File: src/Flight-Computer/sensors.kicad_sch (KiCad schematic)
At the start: 37 parts, among them P4 440054-3, P5 440054-3, P6 440054-3, P7 440054-3, Q1 QS5U17TR, Q2 QS5U17TR, Q3 QS5U17TR, Q4 QS5U17TR, U12 BMM150, U3 BMI323, U4 MAX-8C-0-10, U5 BMP390

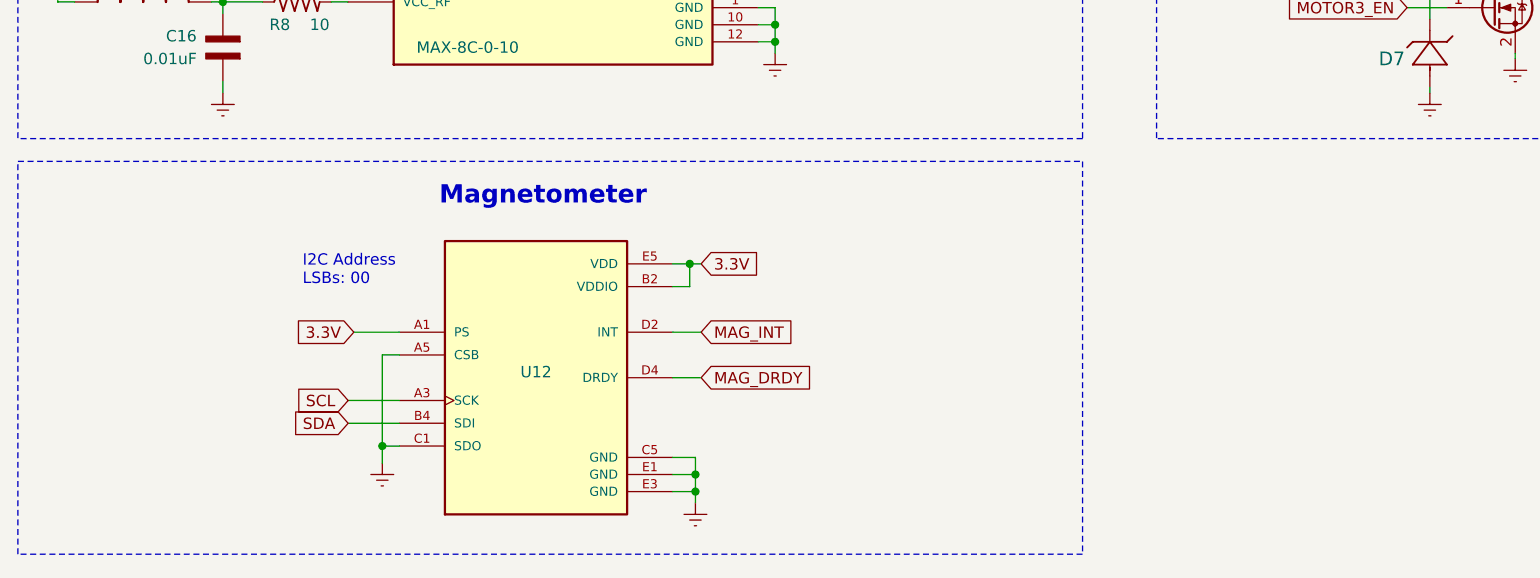
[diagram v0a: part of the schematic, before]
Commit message: PCB Part 1
Changed first part of flight computer to BMM 350 schematic
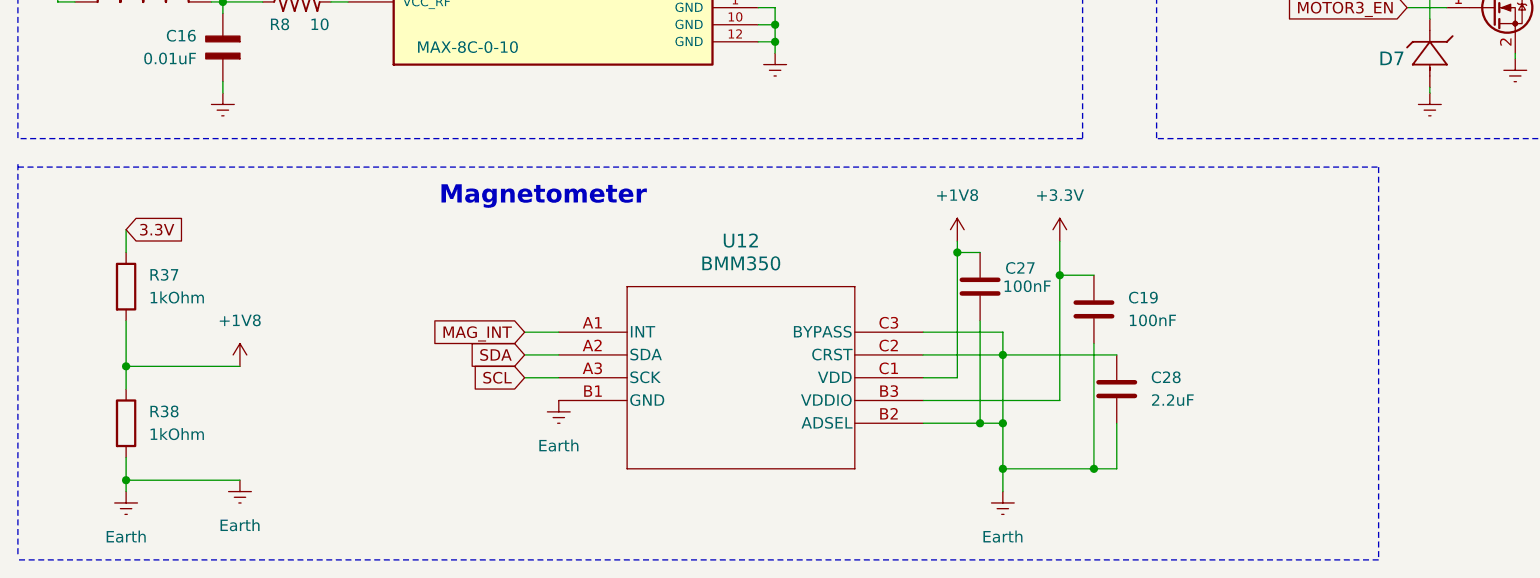
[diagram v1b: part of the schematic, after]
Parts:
- removed U12: BMM150, Flight-Computer:BMM150, symbol Flight-Computer:BMM150
- added C19, C27: 100nF, Capacitor_SMD:C_0201_0603Metric, symbol Device:C
- added C28: 2.2uF, Capacitor_SMD:C_0201_0603Metric, symbol Device:C
- added R37, R38: 1kOhm, Resistor_SMD:R_0201_0603Metric, symbol Device:R
- added U12: BMM350, footprints:BGA9_BMM350_BOS, symbol BMM350:BMM350
- C18: footprint Flight-Computer:CAP_0603 -> Capacitor_SMD:C_0201_0603Metric
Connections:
- net 3.3V: now also R37.1
- net Earth: now also C19.2, C27.2, C28.1, C28.2, R38.2, U12.B1 (GND), U12.B2 (ADSEL), U12.C2 (CRST), U12.C3 (BYPASS)
- net MAG_INT: now also U12.A1 (INT)
- net SCL: now also U12.A3 (SCK)
- net SDA: now also U12.A2 (SDA)
- new net +1V8: C27.1, R37.2, R38.1, U12.C1 (VDD)
- new net +3.3V: C19.1, U12.B3 (VDDIO)
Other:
- note removed: "I2C Address LSBs: 00"

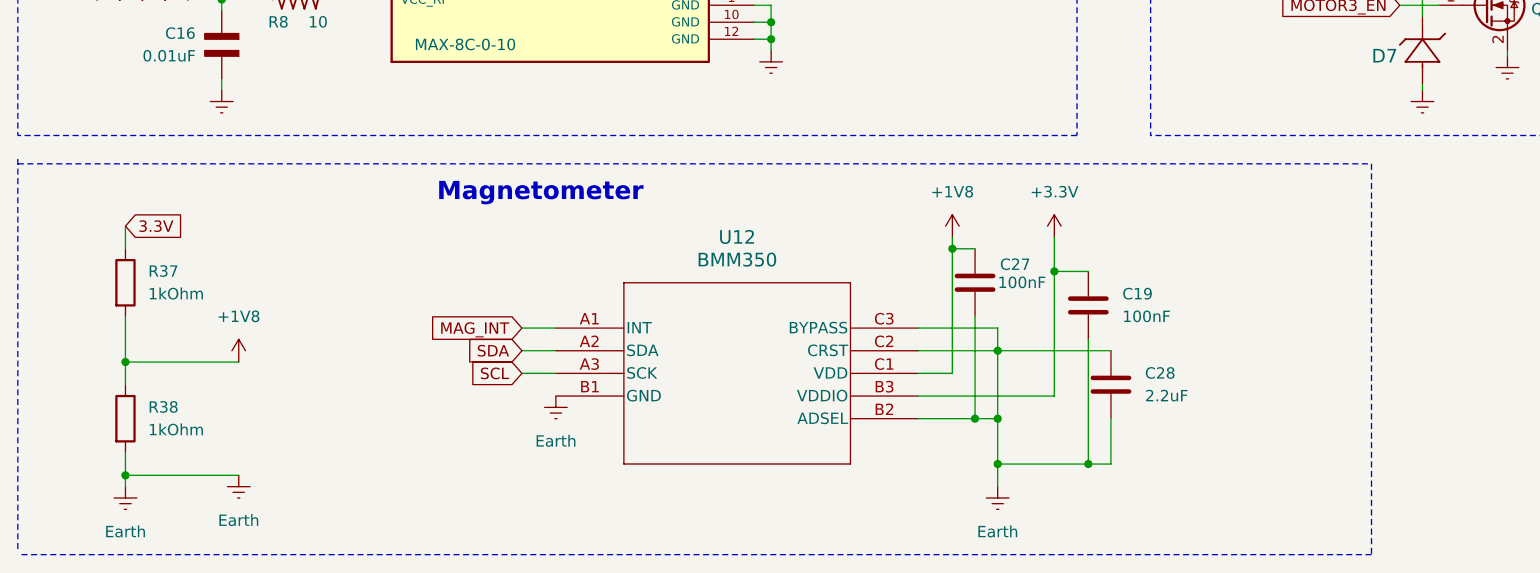
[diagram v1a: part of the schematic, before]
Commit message: S-85S1A
Added S-85S1A to flight computer schematic
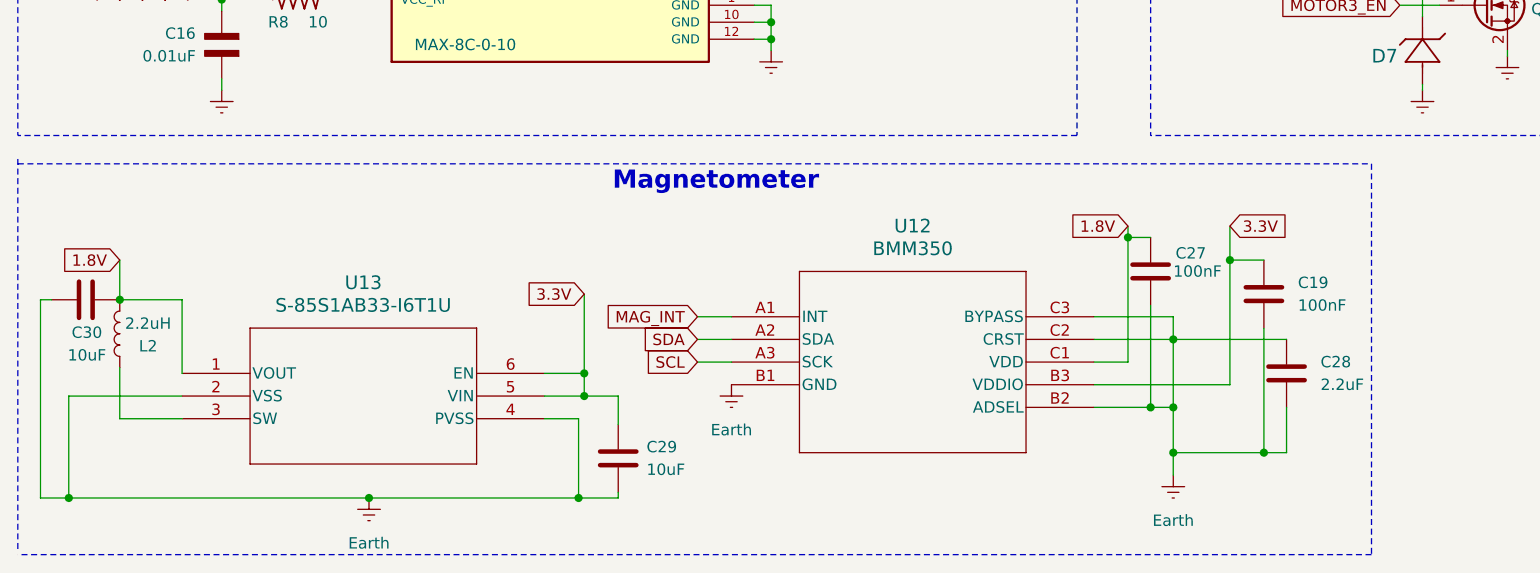
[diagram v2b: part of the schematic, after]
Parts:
- removed R37, R38: 1kOhm, Resistor_SMD:R_0201_0603Metric, symbol Device:R
- added C29, C30: 10uF, Capacitor_SMD:C_0201_0603Metric, symbol Device:C
- added L2: 2.2uH, Inductor_SMD:L_0201_0603Metric, symbol Device:L
- added U13: S-85S1AB33-I6T1U, S85S1A:SNT-6A-A-PKG_PG006-A-P-SD-2.1_ABL, symbol S85S1:S-85S1AB33-I6T1U
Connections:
- net +3.3V is gone; now on net 3.3V: C19.1, U12.B3 (VDDIO)
- net 3.3V: now also C29.1, U13.5 (VIN), U13.6 (EN)
- net Earth: now also C29.2, C30.1, U13.2 (VSS), U13.4 (PVSS)
- net +1V8 renamed 1.8V
- net 1.8V: now also C30.2, L2.2, U13.1 (VOUT)
- new net: L2.1, U13.3 (SW)
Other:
- moved on the sheet: C19, C27, C28, U12

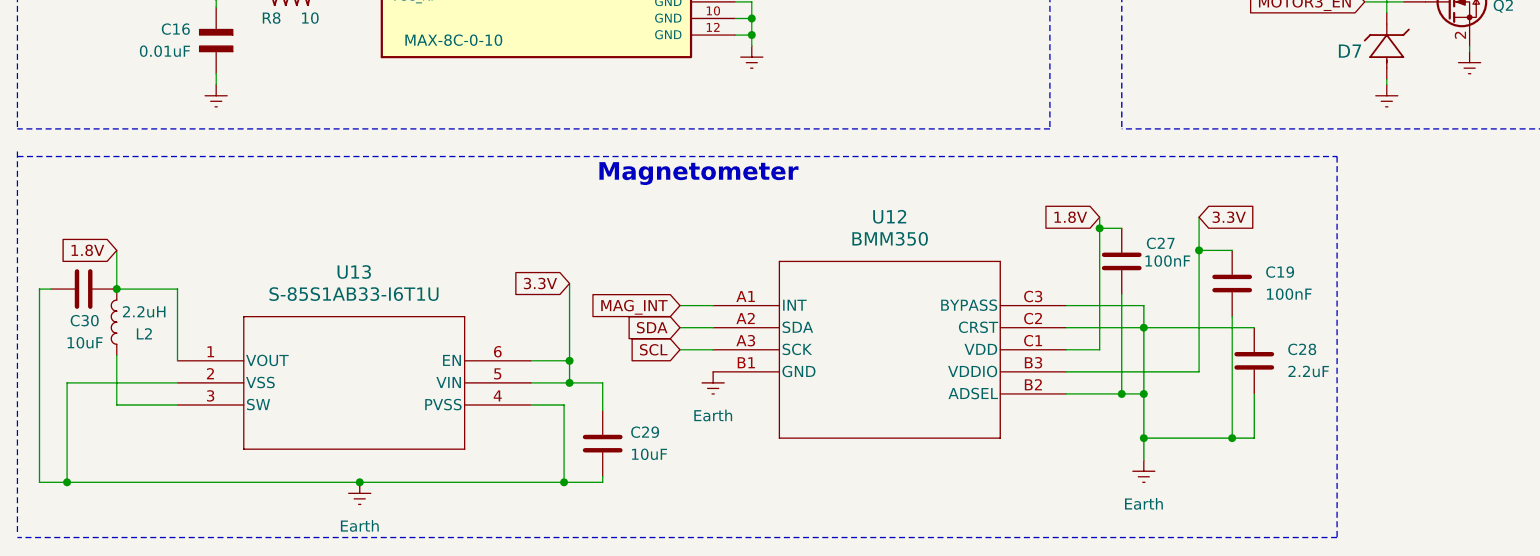
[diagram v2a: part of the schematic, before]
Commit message: quick fix
Fixed BMM350 decoupling capacitor issue
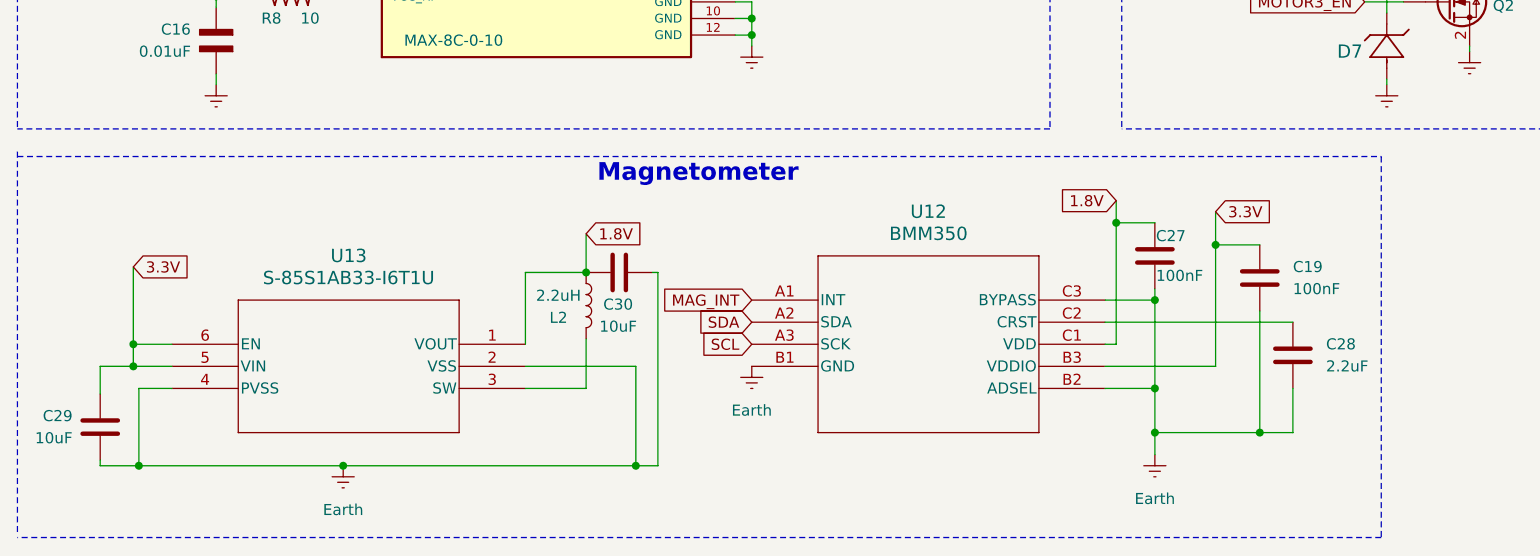
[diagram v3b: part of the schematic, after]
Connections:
- net Earth: no longer C28.1, U12.C2 (CRST)
- new net: C28.1, U12.C2 (CRST)
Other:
- moved on the sheet: C19, C27, C28, C29, C30, L2, U12, U13
